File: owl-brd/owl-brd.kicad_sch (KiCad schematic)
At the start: 53 parts, among them J1 JST, J10 JST, J11 JST, J12 JST, J13 Screw_Terminal_01x02, J14 1x4 Socket, J15 CLTCH1, J16 CLTCH2, J17 CLTCH3, J18 CLTCH4, J19 CLTCH5, J2 JST, J20 CLTCH6, J21 CLTCH7, J22 CLTCH1, J23 Conn_01x03, J24 Conn_01x03, J25 Conn_01x03, J26 Conn_01x03, J27 Screw_Terminal_01x02, J28 JST, J29 Ext Power, J3 JST, J30 Power/UART, J4 JST, J5 JST, J6 JST, J7 JST, J8 JST, J9 JST, Q9 IRLB8721PBF, U1 Pico, U2 L7805CV, U3 TMC2209_SILENTSTEPSTICK, U4 TMC2209_SILENTSTEPSTICK, U5 TMC2209_SILENTSTEPSTICK, U6 TCA9548APWR, U7 74HC238, U8 ULN2803A

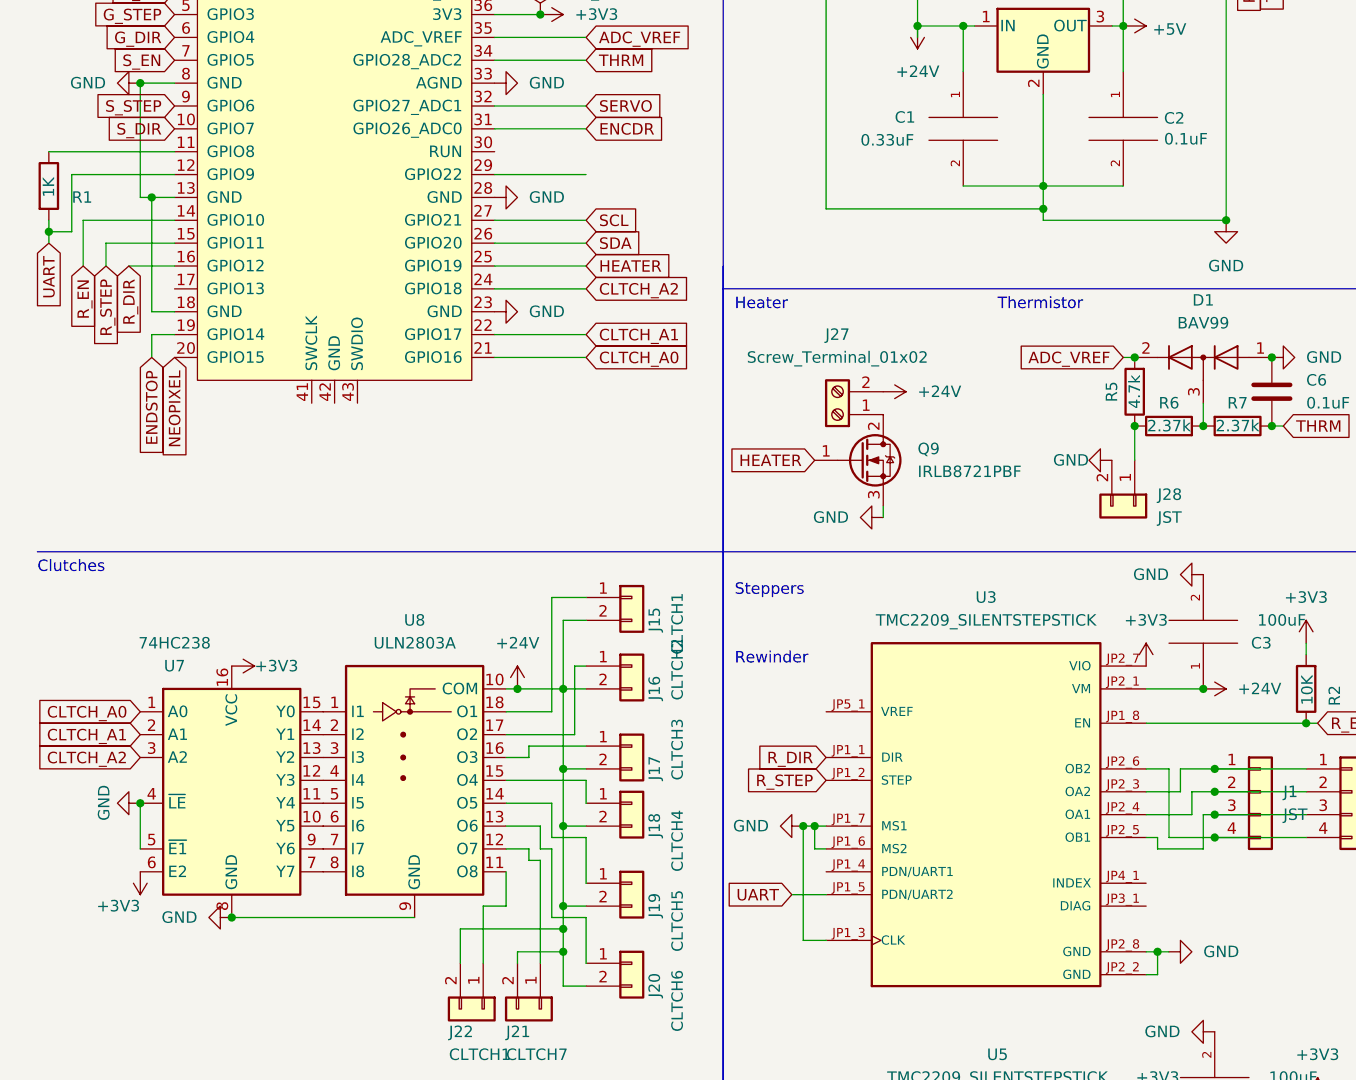
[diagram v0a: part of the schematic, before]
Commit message: - Fix for thermistor mixing vref with 3v3 - Fix footprint for thermistor JST connector - Added enable pin for decoder so that one clutch doesn't have to be on all the time - TODO: rework the CLUTCH pins thickness -- the current thickness may be resulting in a voltage drop and not be sufficient for current
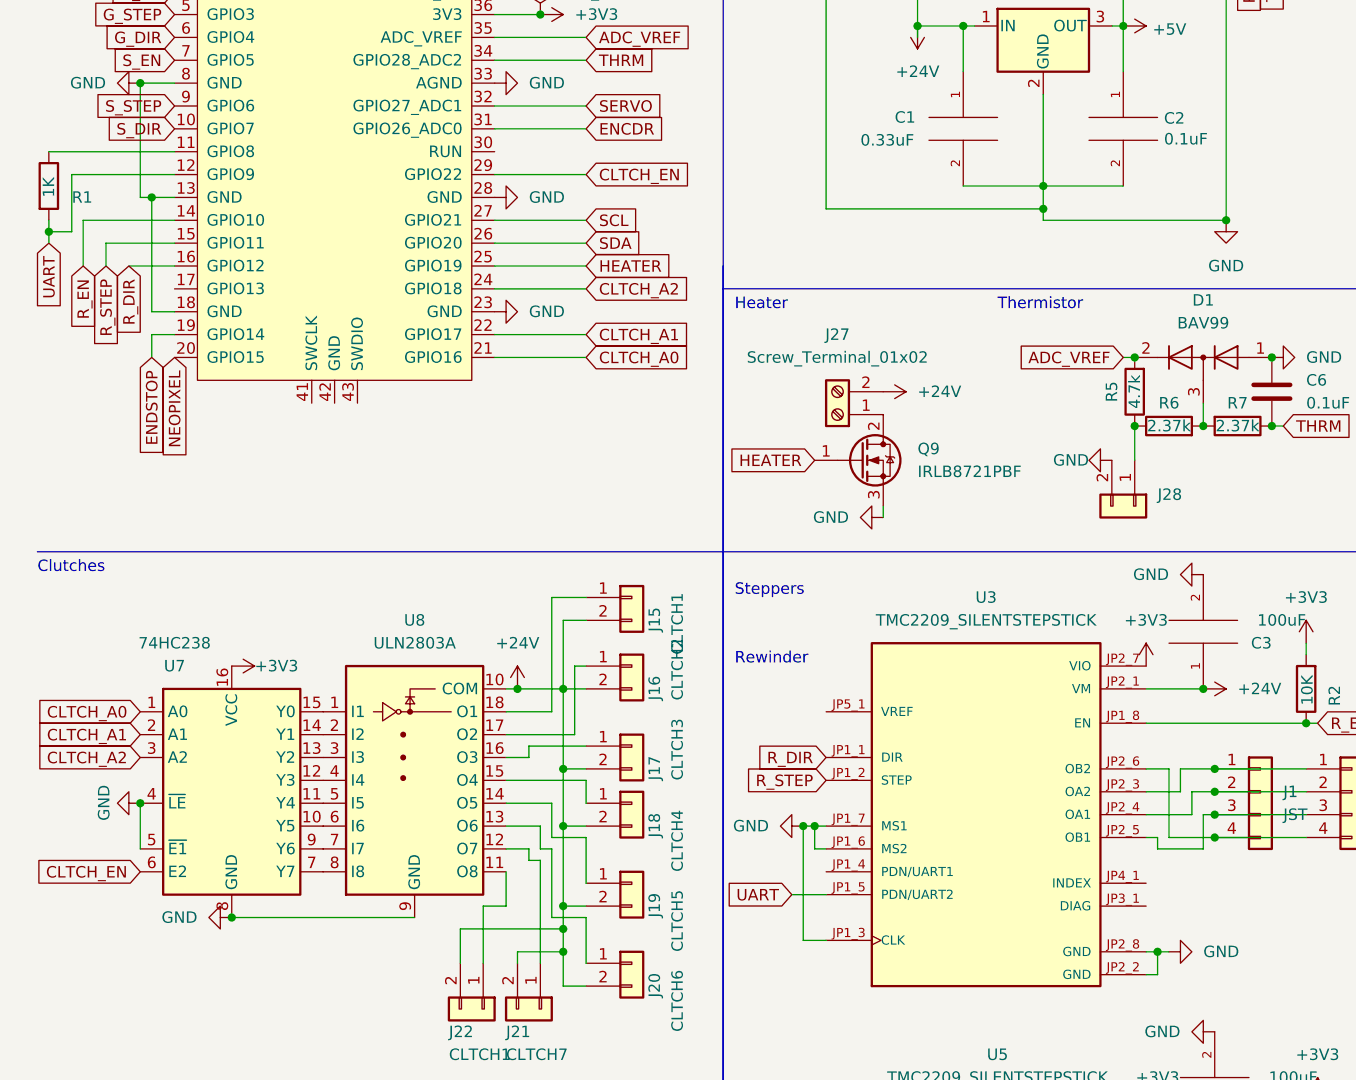
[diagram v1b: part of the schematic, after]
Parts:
- J28: value JST -> (none); footprint Connector_JST:JST_EH_B2B-EH-A_1x02_P2.50mm_Vertical -> (none)
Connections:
- net +3V3: no longer U7.6 (E2)
- net CLTCH_EN: now reaches U1.29 (GPIO22)
- net CLTCH_EN: now also U7.6 (E2)
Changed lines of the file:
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@@
+    )
+  )
+  (global_label "CLTCH_EN" (shape input) (at 24.13 132.08 180) (fields_autoplaced)
+    (effects (font (size 1.27 1.27)) (justify right))
+    (property "Intersheet References" "${INTERSHEET_REFS}" (id 0) (at 12.4036 132.0006 0)
+      (effects (font (size 1.27 1.27)) (justify right) hide)
     )
   )
@@
     (property "Intersheet References" "${INTERSHEET_REFS}" (id 0) (at 93.865 170.1006 0)
       (effects (font (size 1.27 1.27)) (justify right) hide)
+    )
+  )
+  (global_label "CLTCH_EN" (shape input) (at 73.66 54.61 0) (fields_autoplaced)
+    (effects (font (size 1.27 1.27)) (justify left))
+    (property "Intersheet References" "${INTERSHEET_REFS}" (id 0) (at 85.3864 54.5306 0)
+      (effects (font (size 1.27 1.27)) (justify left) hide)
     )
   )
@@
       (effects (font (size 1.27 1.27)) (justify left))
     )
-    (property "Value" "JST" (id 1) (at 137.16 92.7099 90)
-      (effects (font (size 1.27 1.27)) (justify left))
-    )
-    (property "Footprint" "Connector_JST:JST_EH_B2B-EH-A_1x02_P2.50mm_Vertical" (id 2) (at 134.62 91.44 0)
+    (property "Value" "" (id 1) (at 137.16 92.7099 90)
+      (effects (font (size 1.27 1.27)) (justify left))
+    )
+    (property "Footprint" "" (id 2) (at 134.62 91.44 0)
       (effects (font (size 1.27 1.27)) hide)
     )
@@
     )
     (property "Datasheet" "" (id 3) (at 132.08 86.36 0)
-      (effects (font (size 1.27 1.27)) hide)
-    )
-    (pin "1")
-  )
-  (symbol (lib_id "power:+3V3") (at 24.13 132.08 180) (unit 1)
-    (in_bom yes) (on_board yes)
-    (property "Reference" "#PWR0174" (id 0) (at 24.13 128.27 0)
-      (effects (font (size 1.27 1.27)) hide)
-    )
-    (property "Value" "+3V3" (id 1) (at 24.1299 135.89 0)
-      (effects (font (size 1.27 1.27)) (justify left))
-    )
-    (property "Footprint" "" (id 2) (at 24.13 132.08 0)
-      (effects (font (size 1.27 1.27)) hide)
-    )
-    (property "Datasheet" "" (id 3) (at 24.13 132.08 0)
       (effects (font (size 1.27 1.27)) hide)
     )
@@
       (reference "#PWR0173") (unit 1) (value "GND") (footprint "")
     )
-    (path "/e406acf3-684f-44c3-8399-d28232d0eb80"
-      (reference "#PWR0174") (unit 1) (value "+3V3") (footprint "")
-    )
     (path "/5d00bf88-6a42-4aac-8de7-664d1dd07c65"
       (reference "#PWR0175") (unit 1) (value "GND") (footprint "")
@@
     )
     (path "/5cee9003-d22e-4fa3-bf32-34ac3a6b4a2d"
-      (reference "J28") (unit 1) (value "JST") (footprint "Connector_JST:JST_EH_B2B-EH-A_1x02_P2.50mm_Vertical")
+      (reference "J28") (unit 1) (value "JST") (footprint "Connector_JST:JST_XH_B2B-XH-A_1x02_P2.50mm_Vertical")
     )
     (path "/59e087d0-09b4-4220-b3f7-47a5a8e74d1c"

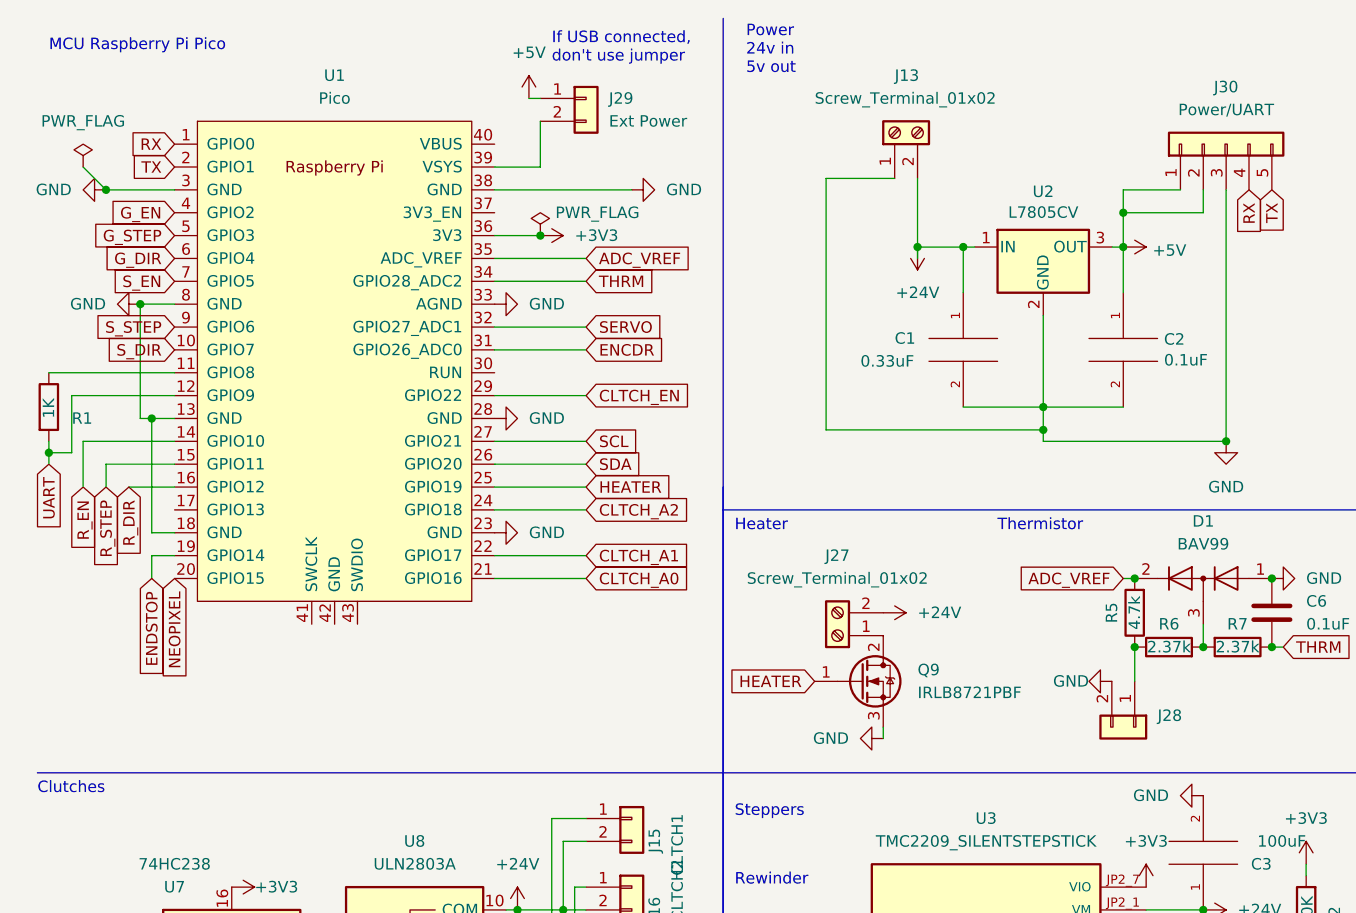
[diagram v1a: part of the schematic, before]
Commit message: -3d models/images -Flipped mosfet -Changed UART order (and labels to match pico rx/tx), in line with Pi and SKR headers
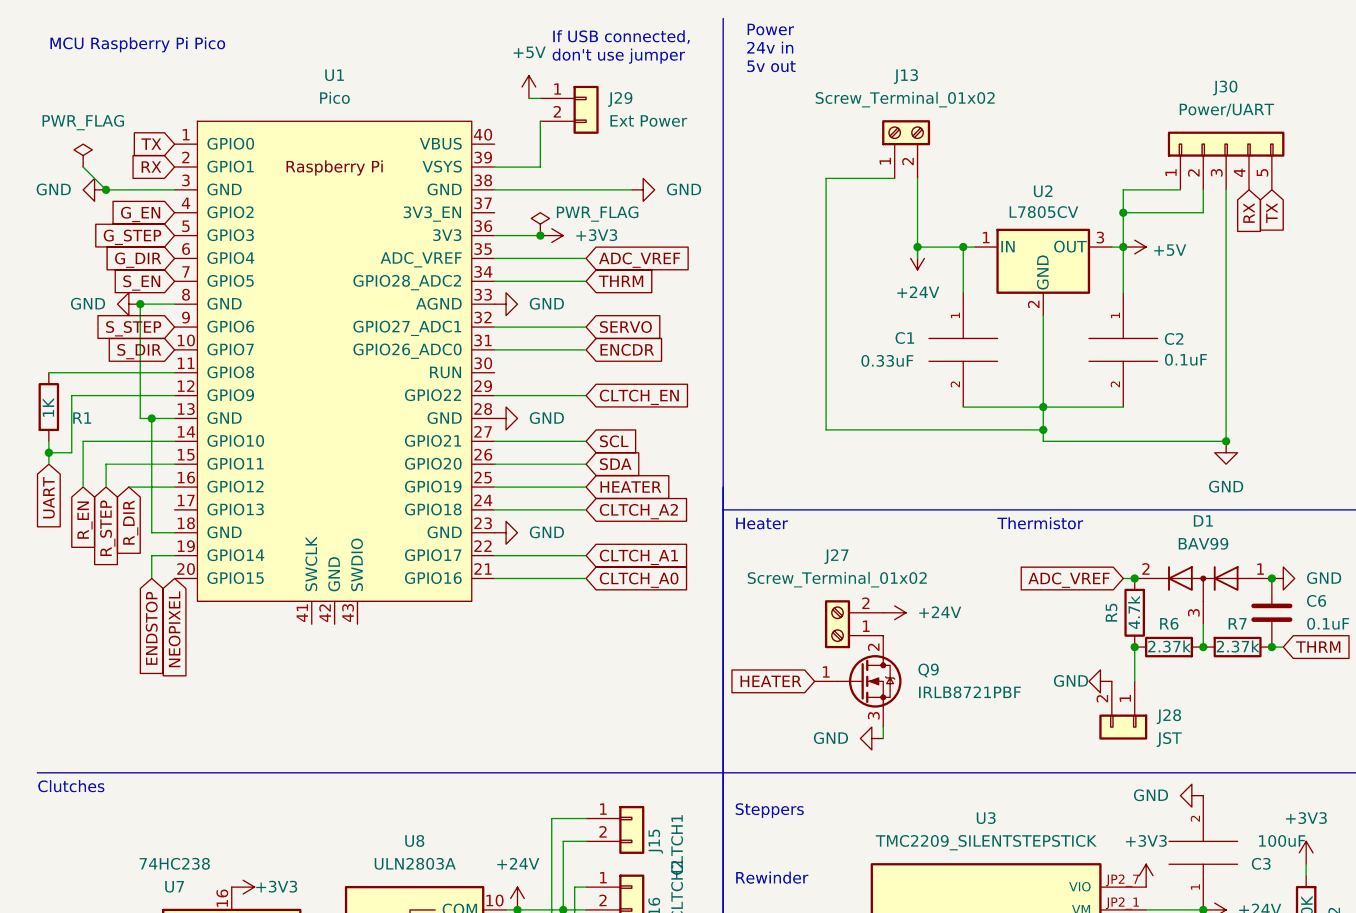
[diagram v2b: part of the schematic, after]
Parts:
- J28: value (none) -> JST; footprint (none) -> Connector_JST:JST_XH_B2B-XH-A_1x02_P2.50mm_Vertical
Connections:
- net RX: now also U1.2 (GPIO1); no longer U1.1 (GPIO0)
- net TX: now also U1.1 (GPIO0); no longer U1.2 (GPIO1)
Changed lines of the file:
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@@
     )
   )
-  (global_label "RX" (shape input) (at 27.94 26.67 180) (fields_autoplaced)
-    (effects (font (size 1.27 1.27)) (justify right))
-    (property "Intersheet References" "${INTERSHEET_REFS}" (id 0) (at 23.0474 26.5906 0)
+  (global_label "TX" (shape input) (at 27.94 26.67 180) (fields_autoplaced)
+    (effects (font (size 1.27 1.27)) (justify right))
+    (property "Intersheet References" "${INTERSHEET_REFS}" (id 0) (at 23.3498 26.5906 0)
       (effects (font (size 1.27 1.27)) (justify right) hide)
     )
@@
     )
   )
-  (global_label "TX" (shape input) (at 27.94 29.21 180) (fields_autoplaced)
-    (effects (font (size 1.27 1.27)) (justify right))
-    (property "Intersheet References" "${INTERSHEET_REFS}" (id 0) (at 23.3498 29.1306 0)
+  (global_label "RX" (shape input) (at 27.94 29.21 180) (fields_autoplaced)
+    (effects (font (size 1.27 1.27)) (justify right))
+    (property "Intersheet References" "${INTERSHEET_REFS}" (id 0) (at 23.0474 29.1306 0)
       (effects (font (size 1.27 1.27)) (justify right) hide)
     )
@@
       (effects (font (size 1.27 1.27)) (justify left))
     )
-    (property "Value" "" (id 1) (at 137.16 92.7099 90)
-      (effects (font (size 1.27 1.27)) (justify left))
-    )
-    (property "Footprint" "" (id 2) (at 134.62 91.44 0)
-      (effects (font (size 1.27 1.27)) hide)
-    )
+    (property "Value" "JST" (id 1) (at 137.16 92.7099 90)
+      (effects (font (size 1.27 1.27)) (justify left))
+    )
+    (property "Footprint" "Connector_JST:JST_XH_B2B-XH-A_1x02_P2.50mm_Vertical" (id 2) (at 134.62 91.44 0)
+      (effects (font (size 1.27 1.27)) hide)
+    )
